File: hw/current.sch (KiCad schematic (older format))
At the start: 22 parts, among them J301 Conn_01x02, J302 Conn_01x02, U301 LP2985-5.0, U302 ACS758LCB-100B-PFF-T, U303 MCP6001-OT, U304 ACS758LCB-100B-PFF-T, U305 MCP6001-OT

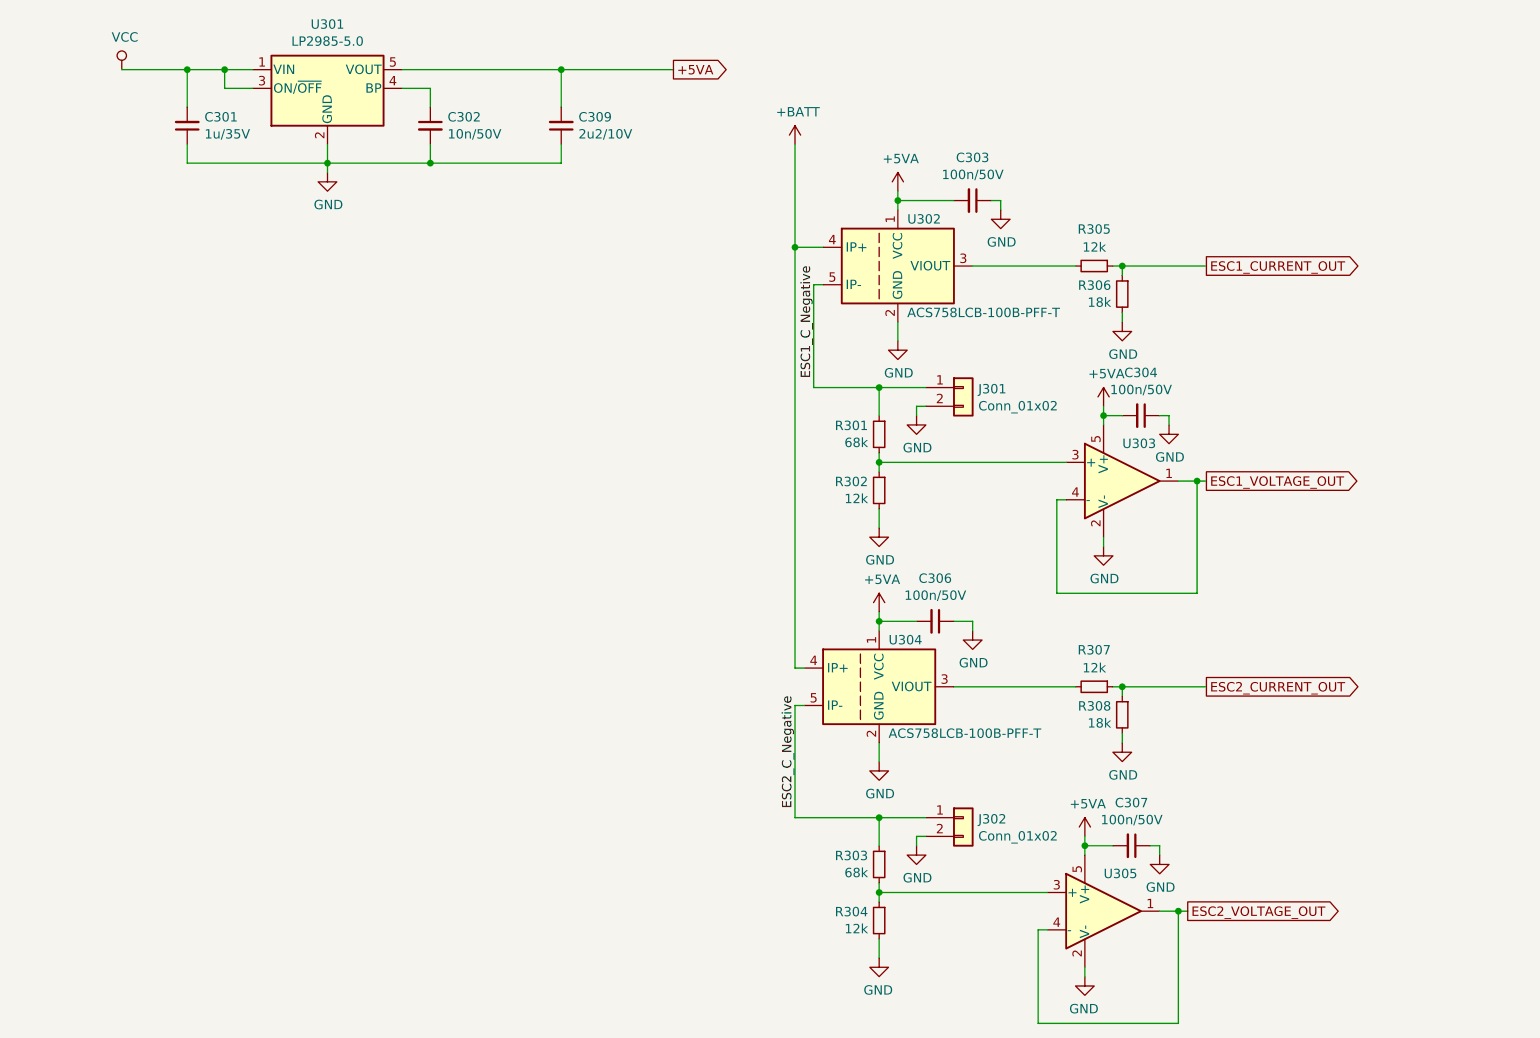
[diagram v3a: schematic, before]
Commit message: Added additional opamp to DAC output as a buffer.
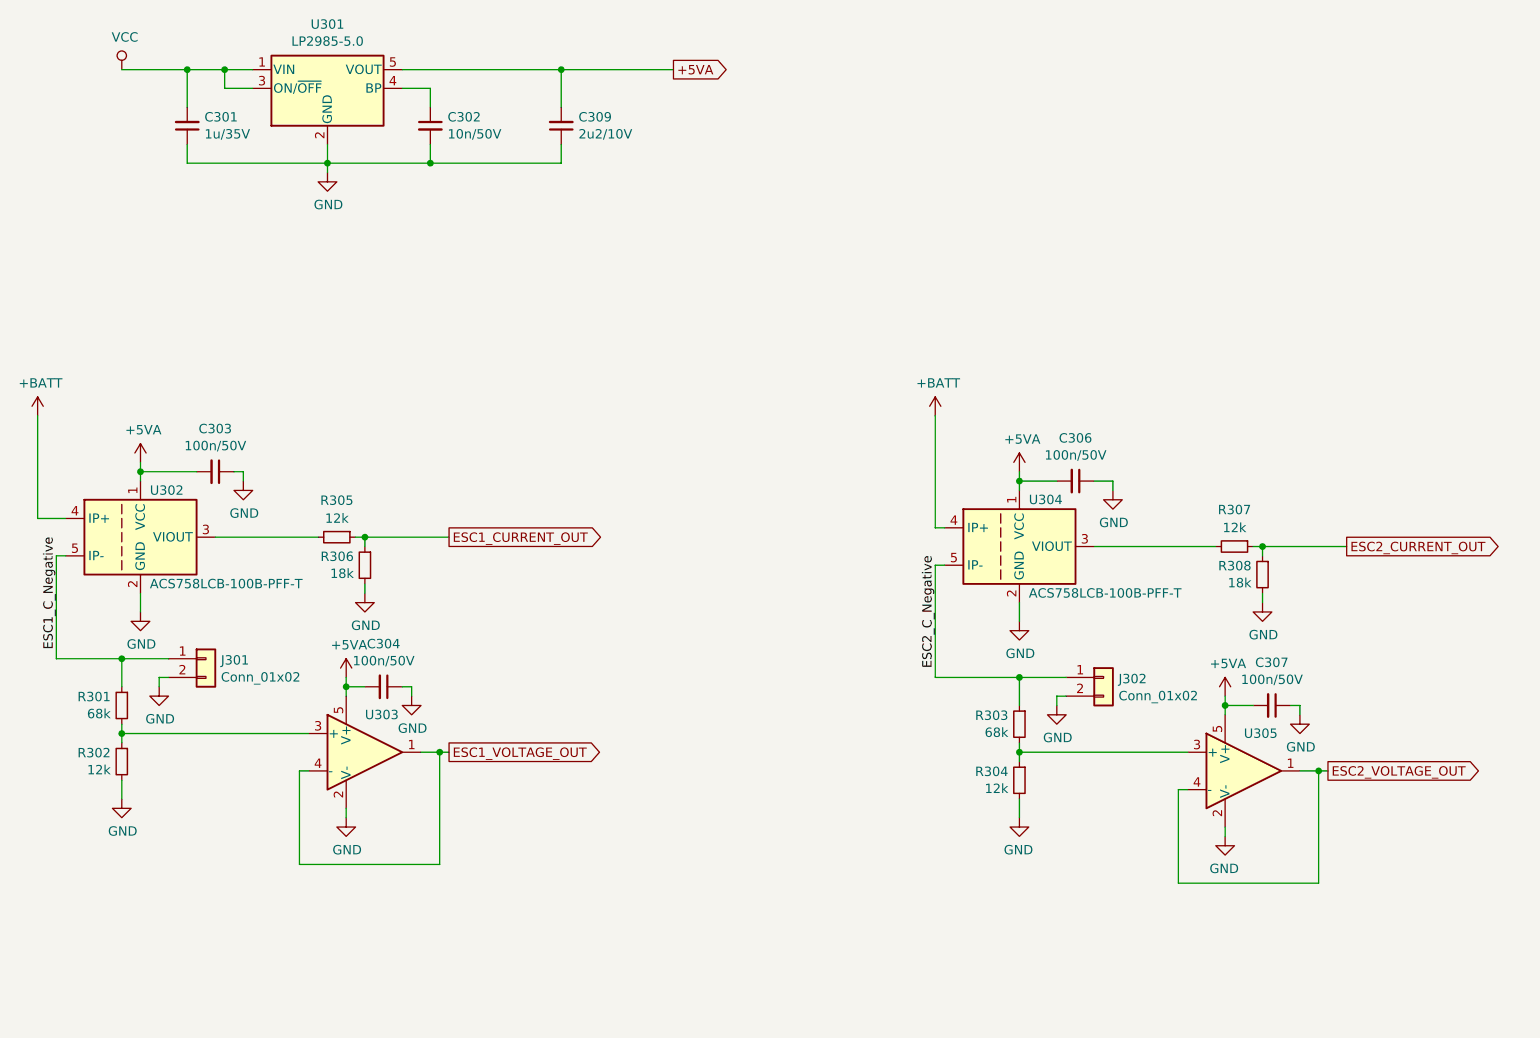
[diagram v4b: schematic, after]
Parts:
- U301, U305: footprint TO_SOT_Packages_SMD:SOT-23-5_HandSoldering -> Package_TO_SOT_SMD:SOT-23-5_HandSoldering
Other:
- moved on the sheet: C303, C304, C306, C307, J301, J302, R301, R302, R303, R304, R305, R306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

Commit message: Fixed Current sensor pinout
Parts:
- U302, U304: footprint PCBDecals:Allegro_PFF -> Sensor_Current:Allegro_CB_PFF
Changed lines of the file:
@@
 F 0 "U302" H 2750 3800 50  0000 L CNN
 F 1 "ACS758LCB-100B-PFF-T" H 2750 3300 50  0000 L CNN
-F 2 "PCBDecals:Allegro_PFF" H 2700 3550 50  0001 C CNN
+F 2 "Sensor_Current:Allegro_CB_PFF" H 2700 3550 50  0001 C CNN
 F 3 "http://www.allegromicro.com/~/media/Files/Datasheets/ACS758-Datasheet.ashx?la=en" H 2700 3550 50  0001 C CNN
 F 4 "-prod" H 2700 3550 50  0001 C CNN "Config"
@@
 F 0 "U304" H 7450 3850 50  0000 L CNN
 F 1 "ACS758LCB-100B-PFF-T" H 7450 3350 50  0000 L CNN
-F 2 "PCBDecals:Allegro_PFF" H 7400 3600 50  0001 C CNN
+F 2 "Sensor_Current:Allegro_CB_PFF" H 7400 3600 50  0001 C CNN
 F 3 "http://www.allegromicro.com/~/media/Files/Datasheets/ACS758-Datasheet.ashx?la=en" H 7400 3600 50  0001 C CNN
 F 4 "-prod" H 7400 3600 50  0001 C CNN "Config"

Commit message: Design updates
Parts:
- added C305, C308: 10n/50V, Capacitor_SMD:C_0603_1608Metric_Pad1.05x0.95mm_HandSolder, symbol Device:C_Small
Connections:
- net ESC1_CURRENT_OUT: now also C305.1
- net ESC2_CURRENT_OUT: now also C308.1
- net GND: now also C305.2, C308.2
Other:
- moved on the sheet: C304, J301, R301, R302, U303
